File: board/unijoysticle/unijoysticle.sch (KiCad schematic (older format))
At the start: 12 parts, among them IC1 7405, IC2 7405, J1 DB9_Female, J2 DB9_Female, J3 Barrel_Jack, SW1 SW_Push

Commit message: schematic: misc. ground points down
genamed gerber to gerber_pcbway (each fab requires different rules)
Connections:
- wire segments 73 -> 79
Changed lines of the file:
@@
 EESchema Schematic File Version 4
 LIBS:unijoysticle-cache
-EELAYER 26 0
+EELAYER 29 0
 EELAYER END
 $Descr A4 11693 8268
@@
 Text GLabel 1150 1100 0    50   Input ~ 0
 GPIO_J1UP
-$Comp
-L power:GND #PWR06
-U 1 1 5C6919E6
-P 1200 7400
-F 0 "#PWR06" H 1200 7150 50  0001 C CNN
-F 1 "GND" V 1205 7272 50  0000 R CNN
-F 2 "" H 1200 7400 50  0001 C CNN
-F 3 "" H 1200 7400 50  0001 C CNN
-	1    1200 7400
-	0    -1   -1   0
-$EndComp
 Wire Wire Line
 	1200 7200 1450 7200
@@
 Text GLabel 8700 5100 0    50   Input ~ 0
 GPIO_J1POTY
-$Comp
-L power:GND #PWR0102
-U 1 1 5C6B262F
-P 4150 1400
-F 0 "#PWR0102" H 4150 1150 50  0001 C CNN
-F 1 "GND" V 4155 1272 50  0000 R CNN
-F 2 "" H 4150 1400 50  0001 C CNN
-F 3 "" H 4150 1400 50  0001 C CNN
-	1    4150 1400
-	0    1    1    0
-$EndComp
 Text GLabel 6150 4600 2    50   Input ~ 0
 GPIO_J1POTX
@@
 Text GLabel 4550 1500 0    50   Input ~ 0
 J1RIGHT
-Wire Wire Line
-	4850 1400 4150 1400
 Text GLabel 6800 950  2    50   Input ~ 0
 J2UP
@@
 L power:GND #PWR0107
 U 1 1 5C6BCB4E
-P 4300 5100
-F 0 "#PWR0107" H 4300 4850 50  0001 C CNN
-F 1 "GND" V 4305 4927 50  0000 C CNN
-F 2 "" H 4300 5100 50  0001 C CNN
-F 3 "" H 4300 5100 50  0001 C CNN
-	1    4300 5100
-	0    1    1    0
+P 4500 5200
+F 0 "#PWR0107" H 4500 4950 50  0001 C CNN
+F 1 "GND" H 4505 5027 50  0000 C CNN
+F 2 "" H 4500 5200 50  0001 C CNN
+F 3 "" H 4500 5200 50  0001 C CNN
+	1    4500 5200
+	1    0    0    -1
 $EndComp
 $Comp
@@
 	5750 4300 6150 4300
 Wire Wire Line
-	4300 5100 4750 5100
+	4500 5100 4750 5100
 Wire Wire Line
 	4300 5000 4750 5000
@@
 	6800 1550 6650 1550
 Wire Wire Line
-	6650 1450 7350 1450
-$Comp
-L power:GND #PWR0108
-U 1 1 5C7111C5
-P 7350 1450
-F 0 "#PWR0108" H 7350 1200 50  0001 C CNN
-F 1 "GND" V 7355 1322 50  0000 R CNN
-F 2 "" H 7350 1450 50  0001 C CNN
-F 3 "" H 7350 1450 50  0001 C CNN
-	1    7350 1450
-	0    -1   -1   0
-$EndComp
-Wire Wire Line
 	5750 3800 6150 3800
 Wire Wire Line
@@
 Wire Wire Line
 	1900 4700 1900 4800
-Wire Wire Line
-	1900 5350 1900 5500
-Wire Wire Line
-	1900 5500 2400 5500
 $Comp
 L power:GND #PWR0101
 U 1 1 5C869C5D
-P 2400 5500
-F 0 "#PWR0101" H 2400 5250 50  0001 C CNN
-F 1 "GND" V 2405 5372 50  0000 R CNN
-F 2 "" H 2400 5500 50  0001 C CNN
-F 3 "" H 2400 5500 50  0001 C CNN
-	1    2400 5500
-	0    -1   -1   0
-$EndComp
-Wire Wire Line
-	9450 5350 9450 5500
-Wire Wire Line
-	9450 5500 10000 5500
+P 1900 5600
+F 0 "#PWR0101" H 1900 5350 50  0001 C CNN
+F 1 "GND" V 1905 5472 50  0000 R CNN
+F 2 "" H 1900 5600 50  0001 C CNN
+F 3 "" H 1900 5600 50  0001 C CNN
+	1    1900 5600
+	1    0    0    -1
+$EndComp
+Wire Wire Line
+	9450 5350 9450 5650
 Wire Wire Line
 	9450 4800 9450 4700
@@
 $EndComp
 $Comp
-L power:GND #PWR0109
-U 1 1 5C86D7BE
-P 10000 5500
-F 0 "#PWR0109" H 10000 5250 50  0001 C CNN
-F 1 "GND" V 10005 5372 50  0000 R CNN
-F 2 "" H 10000 5500 50  0001 C CNN
-F 3 "" H 10000 5500 50  0001 C CNN
-	1    10000 5500
-	0    -1   -1   0
-$EndComp
-$Comp
 L Device:LED D1
 U 1 1 5C86DF58
@@
 Wire Wire Line
 	3650 6200 3400 6200
-$Comp
-L power:GND #PWR0112
-U 1 1 5C87664B
-P 3400 5800
-F 0 "#PWR0112" H 3400 5550 50  0001 C CNN
-F 1 "GND" V 3405 5672 50  0000 R CNN
-F 2 "" H 3400 5800 50  0001 C CNN
-F 3 "" H 3400 5800 50  0001 C CNN
-	1    3400 5800
-	0    1    1    0
-$EndComp
-$Comp
-L power:GND #PWR0113
-U 1 1 5C8766C4
-P 3400 6200
-F 0 "#PWR0113" H 3400 5950 50  0001 C CNN
-F 1 "GND" V 3405 6072 50  0000 R CNN
-F 2 "" H 3400 6200 50  0001 C CNN
-F 3 "" H 3400 6200 50  0001 C CNN
-	1    3400 6200
-	0    1    1    0
-$EndComp
 Wire Wire Line
 	4000 6750 4200 6750
-$Comp
-L power:GND #PWR0114
-U 1 1 5C879807
-P 3400 6750
-F 0 "#PWR0114" H 3400 6500 50  0001 C CNN
-F 1 "GND" V 3405 6622 50  0000 R CNN
-F 2 "" H 3400 6750 50  0001 C CNN
-F 3 "" H 3400 6750 50  0001 C CNN
-	1    3400 6750
-	0    1    1    0
-$EndComp
 Wire Wire Line
 	3400 6750 3600 6750
@@
 Wire Wire Line
 	4450 6200 4600 6200
+Wire Wire Line
+	6650 1450 6750 1450
+Wire Wire Line
+	6750 1450 6750 2000
+Wire Wire Line
+	4850 1400 4750 1400
+Wire Wire Line
+	4750 1400 4750 2000
+$Comp
+L power:GND #PWR?
+U 1 1 5C8CE940
+P 4750 2000
+F 0 "#PWR?" H 4750 1750 50  0001 C CNN
+F 1 "GND" H 4755 1827 50  0000 C CNN
+F 2 "" H 4750 2000 50  0001 C CNN
+F 3 "" H 4750 2000 50  0001 C CNN
+	1    4750 2000
+	1    0    0    -1
+$EndComp
+$Comp
+L power:GND #PWR?
+U 1 1 5C8CEFE9
+P 6750 2000
+F 0 "#PWR?" H 6750 1750 50  0001 C CNN
+F 1 "GND" H 6755 1827 50  0000 C CNN
+F 2 "" H 6750 2000 50  0001 C CNN
+F 3 "" H 6750 2000 50  0001 C CNN
+	1    6750 2000
+	1    0    0    -1
+$EndComp
+Wire Wire Line
+	1900 5350 1900 5600
+Wire Wire Line
+	3400 5800 3400 6200
+Wire Wire Line
+	3400 6200 3400 6750
+Connection ~ 3400 6200
+Wire Wire Line
+	3400 6750 3400 7000
+Connection ~ 3400 6750
+$Comp
+L power:GND #PWR?
+U 1 1 5C8DE08B
+P 3400 7000
+F 0 "#PWR?" H 3400 6750 50  0001 C CNN
+F 1 "GND" H 3405 6827 50  0000 C CNN
+F 2 "" H 3400 7000 50  0001 C CNN
+F 3 "" H 3400 7000 50  0001 C CNN
+	1    3400 7000
+	1    0    0    -1
+$EndComp
+Wire Wire Line
+	1200 7400 1500 7400
+Wire Wire Line
+	1500 7400 1500 7500
+$Comp
+L power:GND #PWR?
+U 1 1 5C8E1CB8
+P 1500 7500
+F 0 "#PWR?" H 1500 7250 50  0001 C CNN
+F 1 "GND" H 1505 7327 50  0000 C CNN
+F 2 "" H 1500 7500 50  0001 C CNN
+F 3 "" H 1500 7500 50  0001 C CNN
+	1    1500 7500
+	1    0    0    -1
+$EndComp
+$Comp
+L power:GND #PWR?
+U 1 1 5C8E2BC0
+P 9450 5650
+F 0 "#PWR?" H 9450 5400 50  0001 C CNN
+F 1 "GND" H 9455 5477 50  0000 C CNN
+F 2 "" H 9450 5650 50  0001 C CNN
+F 3 "" H 9450 5650 50  0001 C CNN
+	1    9450 5650
+	1    0    0    -1
+$EndComp
+Wire Wire Line
+	4500 5100 4500 5200
 $EndSCHEMATC

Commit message: board: renamed 'Parts' -> 'Unijoysticle'
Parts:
- B1: footprint Parts:MH-ET_LIVE_MINIKIT_ESP32 -> Unijoysticle:MH-ET_LIVE_MINIKIT_ESP32
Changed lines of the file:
@@
 F 0 "B1" H 5250 5560 45  0000 C CNN
 F 1 "ESP32_THING_W_ANT_KEEPOUT" H 5250 5476 45  0000 C CNN
-F 2 "Parts:MH-ET_LIVE_MINIKIT_ESP32" H 5250 5400 20  0001 C CNN
+F 2 "Unijoysticle:MH-ET_LIVE_MINIKIT_ESP32" H 5250 5400 20  0001 C CNN
 F 3 "" H 5250 4200 50  0001 C CNN
 F 4 "DEV-13907" H 5250 5381 60  0000 C CNN "Field4"
@@
 	4500 5100 4750 5100
 Wire Wire Line
-	4300 5000 4750 5000
+	4500 5000 4750 5000
 $Comp
 L power:VDD #PWR0103
@@
 F 3 "" H 1950 7200 50  0001 C CNN
 	1    1950 7200
-	0    1    1    0
+	1    0    0    -1
 $EndComp
 $Comp
@@
 L power:VDD #PWR0104
 U 1 1 5C703EAD
-P 4300 5000
-F 0 "#PWR0104" H 4300 4850 50  0001 C CNN
-F 1 "VDD" V 4318 5127 50  0000 L CNN
-F 2 "" H 4300 5000 50  0001 C CNN
-F 3 "" H 4300 5000 50  0001 C CNN
-	1    4300 5000
-	0    -1   -1   0
+P 4500 5000
+F 0 "#PWR0104" H 4500 4850 50  0001 C CNN
+F 1 "VDD" V 4518 5127 50  0000 L CNN
+F 2 "" H 4500 5000 50  0001 C CNN
+F 3 "" H 4500 5000 50  0001 C CNN
+	1    4500 5000
+	1    0    0    -1
 $EndComp
 Wire Wire Line
@@
 Wire Wire Line
 	2450 4300 2650 4300
-$Comp
-L 74xx_IEEE:7405 IC1
-U 6 1 5C88A6AA
-P 1900 5100
-F 0 "IC1" H 1900 5616 50  0000 C CNN
-F 1 "7405" H 1900 5525 50  0000 C CNN
-F 2 "Package_DIP:DIP-14_W7.62mm_LongPads" H 1900 5100 50  0001 C CNN
-F 3 "" H 1900 5100 50  0001 C CNN
-	6    1900 5100
-	1    0    0    -1
-$EndComp
 Text GLabel 1150 5100 0    50   Input ~ 0
 GPIO_J1POTX
@@
 F 3 "" H 2350 4700 50  0001 C CNN
 	1    2350 4700
-	0    1    1    0
+	1    0    0    -1
 $EndComp
 Wire Wire Line
@@
 F 3 "" H 10000 4700 50  0001 C CNN
 	1    10000 4700
-	0    1    1    0
+	1    0    0    -1
 $EndComp
 $Comp
@@
 	4750 1400 4750 2000
 $Comp
-L power:GND #PWR?
+L power:GND #PWR0102
 U 1 1 5C8CE940
 P 4750 2000
-F 0 "#PWR?" H 4750 1750 50  0001 C CNN
+F 0 "#PWR0102" H 4750 1750 50  0001 C CNN
 F 1 "GND" H 4755 1827 50  0000 C CNN
 F 2 "" H 4750 2000 50  0001 C CNN
@@
 $EndComp
 $Comp
-L power:GND #PWR?
+L power:GND #PWR0108
 U 1 1 5C8CEFE9
 P 6750 2000
-F 0 "#PWR?" H 6750 1750 50  0001 C CNN
+F 0 "#PWR0108" H 6750 1750 50  0001 C CNN
 F 1 "GND" H 6755 1827 50  0000 C CNN
 F 2 "" H 6750 2000 50  0001 C CNN
@@
 Connection ~ 3400 6750
 $Comp
-L power:GND #PWR?
+L power:GND #PWR0109
 U 1 1 5C8DE08B
 P 3400 7000
-F 0 "#PWR?" H 3400 6750 50  0001 C CNN
+F 0 "#PWR0109" H 3400 6750 50  0001 C CNN
 F 1 "GND" H 3405 6827 50  0000 C CNN
 F 2 "" H 3400 7000 50  0001 C CNN
@@
 	1500 7400 1500 7500
 $Comp
-L power:GND #PWR?
+L power:GND #PWR0110
 U 1 1 5C8E1CB8
 P 1500 7500
-F 0 "#PWR?" H 1500 7250 50  0001 C CNN
+F 0 "#PWR0110" H 1500 7250 50  0001 C CNN
 F 1 "GND" H 1505 7327 50  0000 C CNN
 F 2 "" H 1500 7500 50  0001 C CNN
@@
 $EndComp
 $Comp
-L power:GND #PWR?
+L power:GND #PWR0111
 U 1 1 5C8E2BC0
 P 9450 5650
-F 0 "#PWR?" H 9450 5400 50  0001 C CNN
+F 0 "#PWR0111" H 9450 5400 50  0001 C CNN
 F 1 "GND" H 9455 5477 50  0000 C CNN
 F 2 "" H 9450 5650 50  0001 C CNN
@@
 Wire Wire Line
 	4500 5100 4500 5200
+$Comp
+L 74xx_IEEE:7405 IC1
+U 6 1 5C88A6AA
+P 1900 5100
+F 0 "IC1" H 1900 5616 50  0000 C CNN
+F 1 "7405" H 1900 5525 50  0000 C CNN
+F 2 "Package_DIP:DIP-14_W7.62mm_LongPads" H 1900 5100 50  0001 C CNN
+F 3 "" H 1900 5100 50  0001 C CNN
+	6    1900 5100
+	1    0    0    -1
+$EndComp
 $EndSCHEMATC

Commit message: firmware: uni_gpio
schematic: borders around components
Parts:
- B1: value ESP32_THING_W_ANT_KEEPOUT -> ESP32 MINI KIT
- R1, R2: value R -> 100
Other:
- note added: "7405s: Joystick switches"
- note added: "Barrel Jack"
- note added: "DB9's: Port A, Port B"
- note added: "ESP32"
- note added: "LEDs & Push Button"
- moved on the sheet: D1, D2, D3, IC1A, IC1B, IC1C, IC1D, IC1E, IC1F, IC2A, IC2B, IC2C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

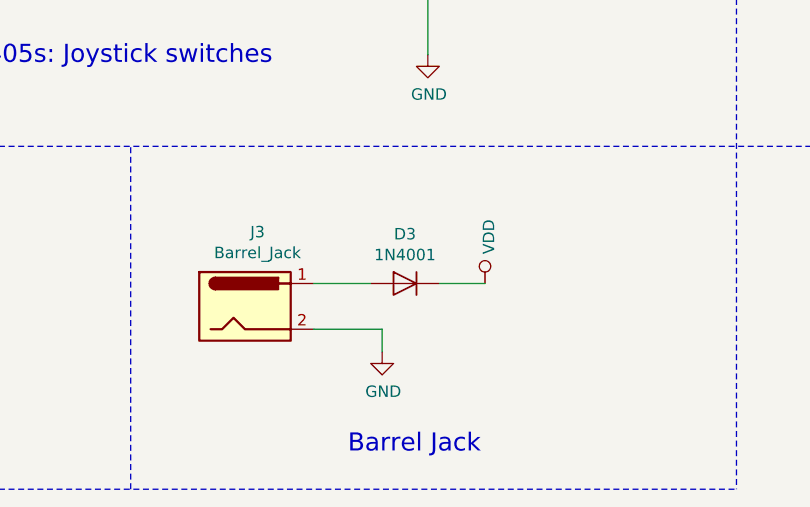
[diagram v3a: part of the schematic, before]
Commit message: firmware: support for new mappings (v2)
board: board slightly bigger, diode smaller, resistrors larger
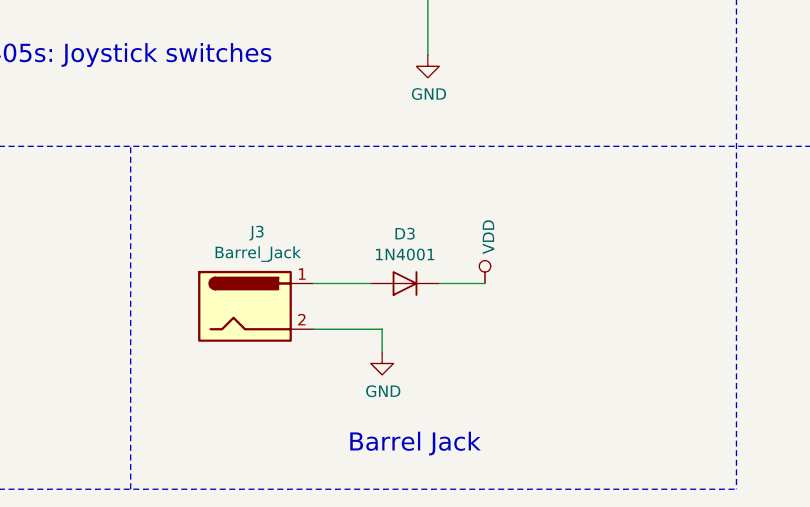
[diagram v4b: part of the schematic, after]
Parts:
- D3: footprint Diode_THT:D_DO-41_SOD81_P10.16mm_Horizontal -> Diode_THT:D_DO-41_SOD81_P7.62mm_Horizontal
- R1, R2: footprint Resistor_THT:R_Axial_DIN0204_L3.6mm_D1.6mm_P5.08mm_Horizontal -> Resistor_THT:R_Axial_DIN0204_L3.6mm_D1.6mm_P7.62mm_Horizontal
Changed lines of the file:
@@
 Sheet 1 1
 Title "Unijoysticle 2"
-Date "2019-03-13"
-Rev "v0.0.1"
+Date "2019-03-28"
+Rev "v0.0.2"
 Comp "Retro Moe"
 Comment1 "Ricardo Quesada"
@@
 Comment4 ""
 $EndDescr
-$Comp
-L Diode:1N4001 D3
-U 1 1 5C65A496
-P 4300 6900
-F 0 "D3" H 4300 7116 50  0000 C CNN
-F 1 "1N4001" H 4300 7025 50  0000 C CNN
-F 2 "Diode_THT:D_DO-41_SOD81_P10.16mm_Horizontal" H 4300 6725 50  0001 C CNN
-F 3 "" H 4300 6900 50  0001 C CNN
-	1    4300 6900
-	-1   0    0    -1
-$EndComp
 Text GLabel 8550 4100 2    50   Input ~ 0
 GPIO_J1UP
@@
 Wire Wire Line
 	6700 4300 7150 4300
-$Comp
-L Device:R R1
-U 1 1 5C87CFE9
-P 1650 6550
-F 0 "R1" V 1443 6550 50  0000 C CNN
-F 1 "100" V 1534 6550 50  0000 C CNN
-F 2 "Resistor_THT:R_Axial_DIN0204_L3.6mm_D1.6mm_P5.08mm_Horizontal" V 1580 6550 50  0001 C CNN
-F 3 "~" H 1650 6550 50  0001 C CNN
-	1    1650 6550
-	0    1    1    0
-$EndComp
-$Comp
-L Device:R R2
-U 1 1 5C87D07A
-P 1650 6950
-F 0 "R2" V 1443 6950 50  0000 C CNN
-F 1 "100" V 1534 6950 50  0000 C CNN
-F 2 "Resistor_THT:R_Axial_DIN0204_L3.6mm_D1.6mm_P5.08mm_Horizontal" V 1580 6950 50  0001 C CNN
-F 3 "~" H 1650 6950 50  0001 C CNN
-	1    1650 6950
-	0    1    1    0
-$EndComp
 Wire Wire Line
 	1800 6550 1950 6550
@@
 Text Notes 4050 7650 0    79   ~ 0
 Barrel Jack
+$Comp
+L Device:R R1
+U 1 1 5C9DFE27
+P 1650 6550
+F 0 "R1" V 1443 6550 50  0000 C CNN
+F 1 "100" V 1534 6550 50  0000 C CNN
+F 2 "Resistor_THT:R_Axial_DIN0204_L3.6mm_D1.6mm_P7.62mm_Horizontal" V 1580 6550 50  0001 C CNN
+F 3 "~" H 1650 6550 50  0001 C CNN
+	1    1650 6550
+	0    1    1    0
+$EndComp
+$Comp
+L Device:R R2
+U 1 1 5C9DF1A9
+P 1650 6950
+F 0 "R2" V 1443 6950 50  0000 C CNN
+F 1 "100" V 1534 6950 50  0000 C CNN
+F 2 "Resistor_THT:R_Axial_DIN0204_L3.6mm_D1.6mm_P7.62mm_Horizontal" V 1580 6950 50  0001 C CNN
+F 3 "~" H 1650 6950 50  0001 C CNN
+	1    1650 6950
+	0    1    1    0
+$EndComp
+$Comp
+L Diode:1N4001 D3
+U 1 1 5CA00191
+P 4300 6900
+F 0 "D3" H 4300 6684 50  0000 C CNN
+F 1 "1N4001" H 4300 6775 50  0000 C CNN
+F 2 "Diode_THT:D_DO-41_SOD81_P7.62mm_Horizontal" H 4300 6725 50  0001 C CNN
+F 3 "http://www.vishay.com/docs/88503/1n4001.pdf" H 4300 6900 50  0001 C CNN
+	1    4300 6900
+	-1   0    0    1
+$EndComp
 $EndSCHEMATC

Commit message: firmware: using GPIOS correctly.
new GPIOS for a some lines so that it doesn't crash
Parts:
- J3: footprint Connector_BarrelJack:BarrelJack_Horizontal -> Unijoysticle:BarrelJack_Horizontal
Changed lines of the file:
@@
 Text GLabel 3650 5350 0    50   Input ~ 0
 GPIO_J1POTY
-Text GLabel 8550 5000 2    50   Input ~ 0
+Text GLabel 8550 4800 2    50   Input ~ 0
 GPIO_J1POTX
 Text GLabel 6700 4000 0    50   Input ~ 0
@@
 $EndComp
 $Comp
-L Connector:Barrel_Jack J3
-U 1 1 5C70344B
-P 3600 7000
-F 0 "J3" H 3655 7325 50  0000 C CNN
-F 1 "Barrel_Jack" H 3655 7234 50  0000 C CNN
-F 2 "Connector_BarrelJack:BarrelJack_Horizontal" H 3650 6960 50  0001 C CNN
-F 3 "" H 3650 6960 50  0001 C CNN
-	1    3600 7000
-	1    0    0    -1
-$EndComp
-$Comp
 L power:VDD #PWR0104
 U 1 1 5C703EAD
@@
 	6700 4000 7150 4000
 Wire Wire Line
-	8550 5000 8150 5000
+	8550 4800 8150 4800
 $Comp
 L 74xx_IEEE:7405 IC1
@@
 Text GLabel 1950 6950 2    50   Input ~ 0
 GPIO_J2LED
-Text GLabel 6700 4700 0    50   Input ~ 0
+Text GLabel 6700 5100 0    50   Input ~ 0
 GPIO_J1LED
 Text GLabel 6700 4300 0    50   Input ~ 0
 GPIO_J2LED
 Wire Wire Line
-	6700 4700 7150 4700
+	6700 5100 7150 5100
 Wire Wire Line
 	6700 4300 7150 4300
@@
 	-1   0    0    1
 $EndComp
+$Comp
+L Connector:Barrel_Jack J3
+U 1 1 5CA09684
+P 3600 7000
+F 0 "J3" H 3657 7325 50  0000 C CNN
+F 1 "Barrel_Jack" H 3657 7234 50  0000 C CNN
+F 2 "Unijoysticle:BarrelJack_Horizontal" H 3650 6960 50  0001 C CNN
+F 3 "~" H 3650 6960 50  0001 C CNN
+	1    3600 7000
+	1    0    0    -1
+$EndComp
 $EndSCHEMATC

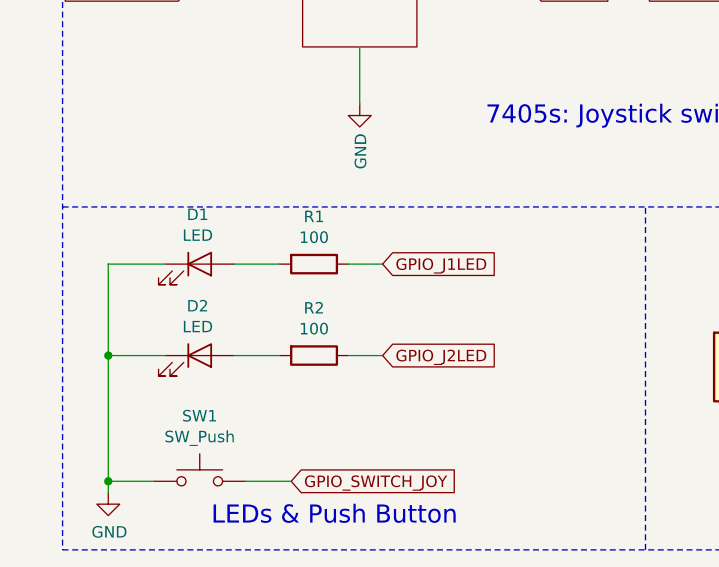
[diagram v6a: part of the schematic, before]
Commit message: board: missing BarrelJack
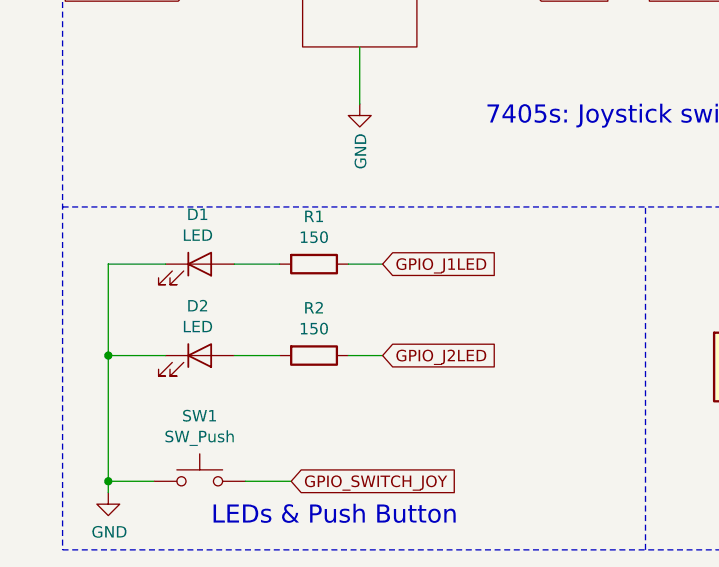
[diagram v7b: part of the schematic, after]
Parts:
- R1, R2: value 100 -> 150
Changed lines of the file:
@@
 P 1650 6550
 F 0 "R1" V 1443 6550 50  0000 C CNN
-F 1 "100" V 1534 6550 50  0000 C CNN
+F 1 "150" V 1534 6550 50  0000 C CNN
 F 2 "Resistor_THT:R_Axial_DIN0204_L3.6mm_D1.6mm_P7.62mm_Horizontal" V 1580 6550 50  0001 C CNN
 F 3 "~" H 1650 6550 50  0001 C CNN
@@
 P 1650 6950
 F 0 "R2" V 1443 6950 50  0000 C CNN
-F 1 "100" V 1534 6950 50  0000 C CNN
+F 1 "150" V 1534 6950 50  0000 C CNN
 F 2 "Resistor_THT:R_Axial_DIN0204_L3.6mm_D1.6mm_P7.62mm_Horizontal" V 1580 6950 50  0001 C CNN
 F 3 "~" H 1650 6950 50  0001 C CNN

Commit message: board: move sparkfun lib inside project
so 3rd party users can see the schematic without any error
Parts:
- B1: symbol SparkFun-Boards:ESP32_THING_W_ANT_KEEPOUT -> unijoysticle-rescue:ESP32_THING_W_ANT_KEEPOUT-SparkFun-Boards
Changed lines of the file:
@@
 $EndComp
 $Comp
-L SparkFun-Boards:ESP32_THING_W_ANT_KEEPOUT B1
+L unijoysticle-rescue:ESP32_THING_W_ANT_KEEPOUT-SparkFun-Boards B1
 U 1 1 5C6B6FCB
 P 7650 4600
